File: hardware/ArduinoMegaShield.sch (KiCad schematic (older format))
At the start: 23 parts, among them P1 CONN_01X02, P10 CONN_01X02, P11 CONN_01X02, P12 CONN_01X02, P13 CONN_01X02, P14 CONN_01X02, P15 CONN_01X02, P16 CONN_01X02, P2 CONN_01X02, P3 CONN_01X02, P4 CONN_01X02, P5 CONN_01X02, P6 CONN_01X02, P7 CONN_01X02, P8 CONN_01X02, P9 CONN_01X02, U1 A4988, U2 A4988, U3 A4988

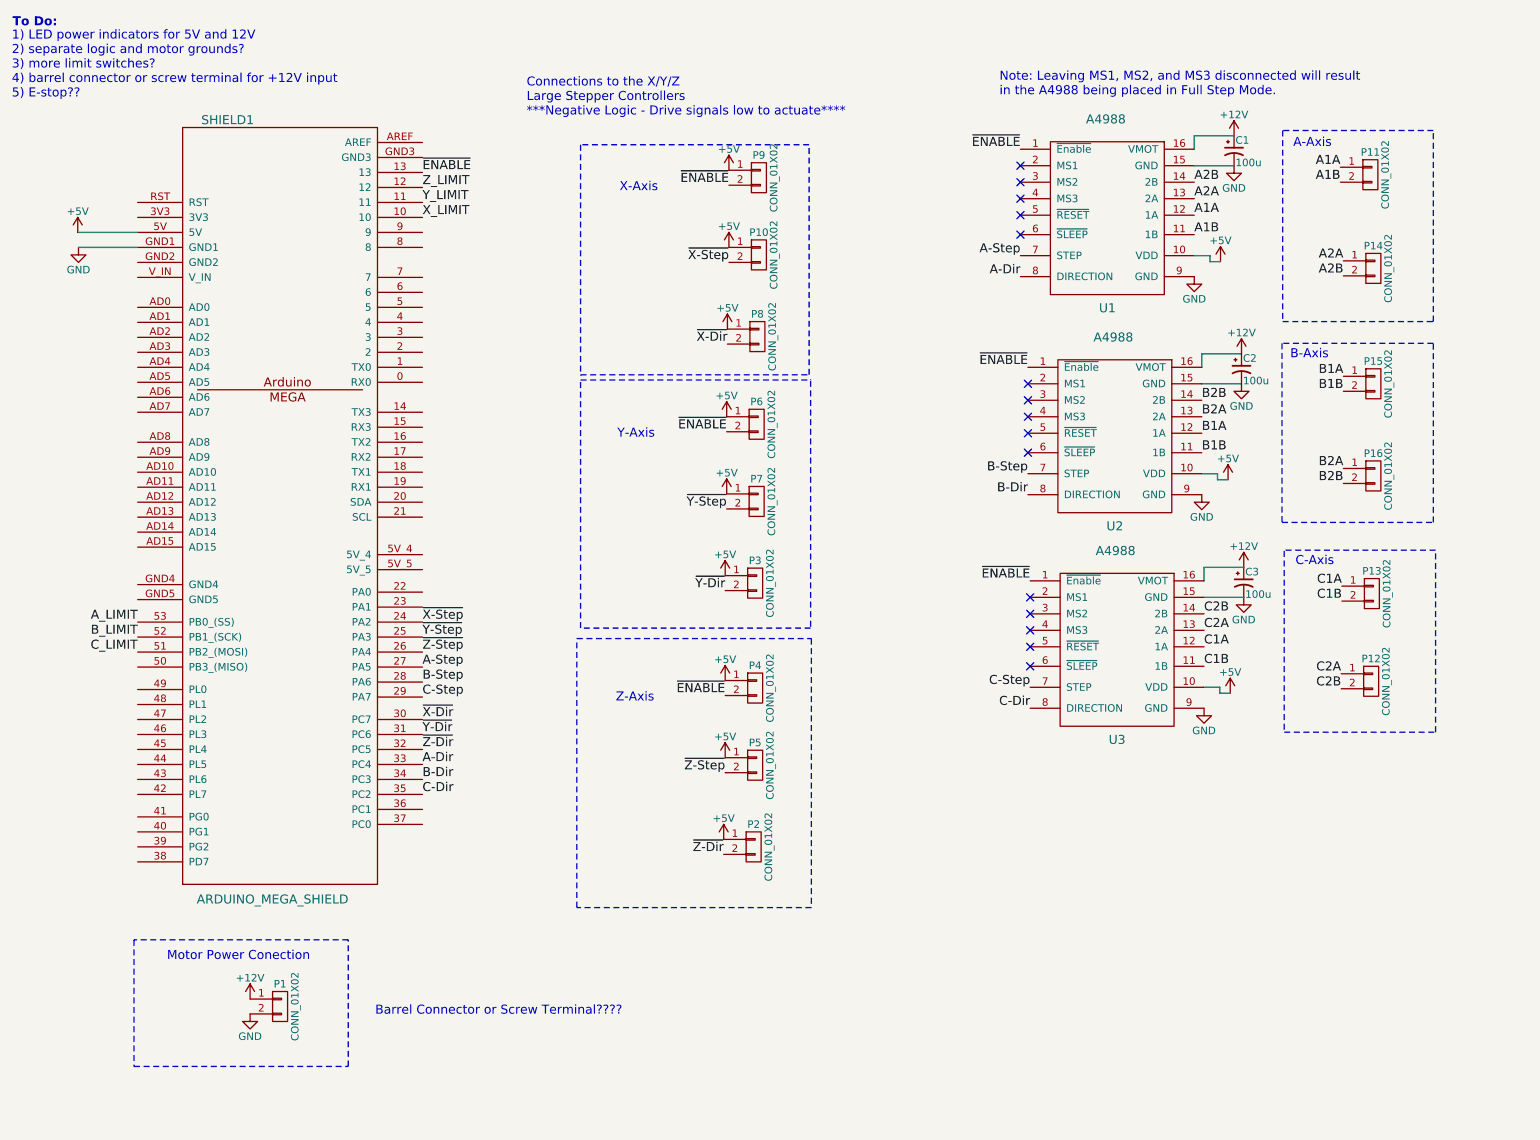
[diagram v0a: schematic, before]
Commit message: added microstepping NOPOP resistors and power indicator LEDs.  Assigned some footprints
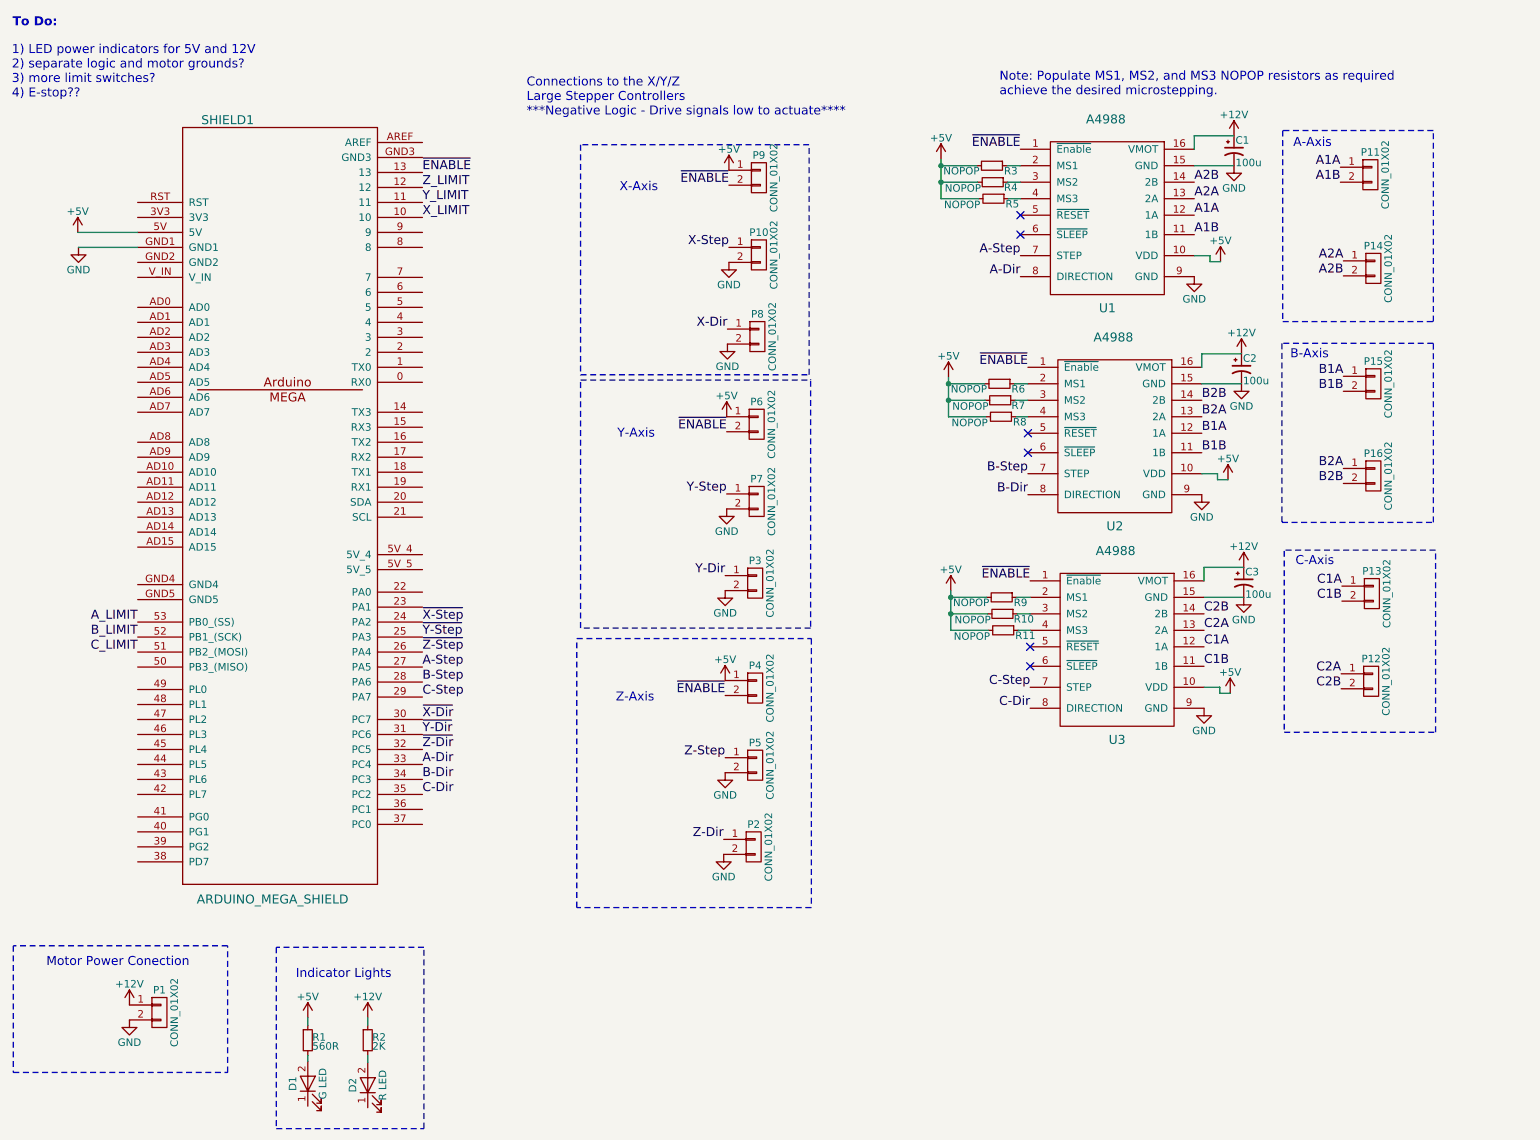
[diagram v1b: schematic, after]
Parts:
- added D1: G LED, LEDs:LED_0805, symbol LED
- added D2: R LED, LEDs:LED_0805, symbol LED
- added R1: 560R, Resistors_SMD:R_0805_HandSoldering, symbol R_Small
- added R10, R11, R3, R4, R5, R6, R7, R8, R9: NOPOP, Resistors_SMD:R_0805_HandSoldering, symbol R_Small
- added R2: 2K, Resistors_SMD:R_0805_HandSoldering, symbol R_Small
- P1, P10, P11, P12, P13, P14, P15, P16, P2, P3, P4, P5, P6, P7, P8, P9: footprint (none) -> Pin_Headers:Pin_Header_Straight_1x02
- SHIELD1: footprint (none) -> arduino-shields:ARDUINO_MEGA_SHIELD
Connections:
- net +12V: now also R2.1
- net +5V: now also R1.1, R10.2, R11.2, R3.2, R4.2, R5.2, R6.2, R7.2, R8.2, R9.2; no longer P10.1 (P1), P2.1 (P1), P3.1 (P1), P5.1 (P1), P7.1 (P1), P8.1 (P1)
- net GND: now also P10.2 (P2), P2.2 (P2), P3.2 (P2), P5.2 (P2), P7.2 (P2), P8.2 (P2)
- net ~X-Dir: no longer P8.2 (P2)
- net ~X-Step: no longer P10.2 (P2)
- net ~Y-Dir: no longer P3.2 (P2)
- net ~Y-Step: no longer P7.2 (P2)
- net ~Z-Dir: no longer P2.2 (P2)
- net ~Z-Step: no longer P5.2 (P2)
- net at U1.2 (MS1): now also R3.1
- net at U1.3 (MS2): now also R4.1
- net at U1.4 (MS3): now also R5.1
- net at U2.2 (MS1): now also R6.1
- net at U2.3 (MS2): now also R7.1
- net at U2.4 (MS3): now also R8.1
- net at U3.2 (MS1): now also R9.1
- net at U3.3 (MS2): now also R10.1
- net at U3.4 (MS3): now also R11.1
- new net: D1.2 (A), R1.2
- new net: D2.2 (A), R2.2
- new net X-Dir: P8.1 (P1)
- new net X-Step: P10.1 (P1)
- new net Y-Dir: P3.1 (P1)
- new net Y-Step: P7.1 (P1)
- new net Z-Dir: P2.1 (P1)
- new net Z-Step: P5.1 (P1)
- no-connect marks 15 -> 6
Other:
- note added: "1) LED power indicators for 5V and 12V\n2) separate logic and motor grounds?\n3) more limit switches?\n4) E-stop??"
- note added: "Indicator Lights"
- note added: "Note: Populate MS1, MS2, and MS3 NOPOP resistors as required\nachieve the desired microstepping."
- note removed: "1) LED power indicators for 5V and 12V\n2) separate logic and motor grounds?\n3) more limit switches?\n4) barrel connector or screw terminal for +12V input\n5) E-stop??"
- note removed: "Barrel Connector or Screw Terminal????"
- note removed: "Note: Leaving MS1, MS2, and MS3 disconnected will result\nin the A4988 being placed in Full Step Mode."
- moved on the sheet: P1

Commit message: correctly logic of steps/dir on shield output pins
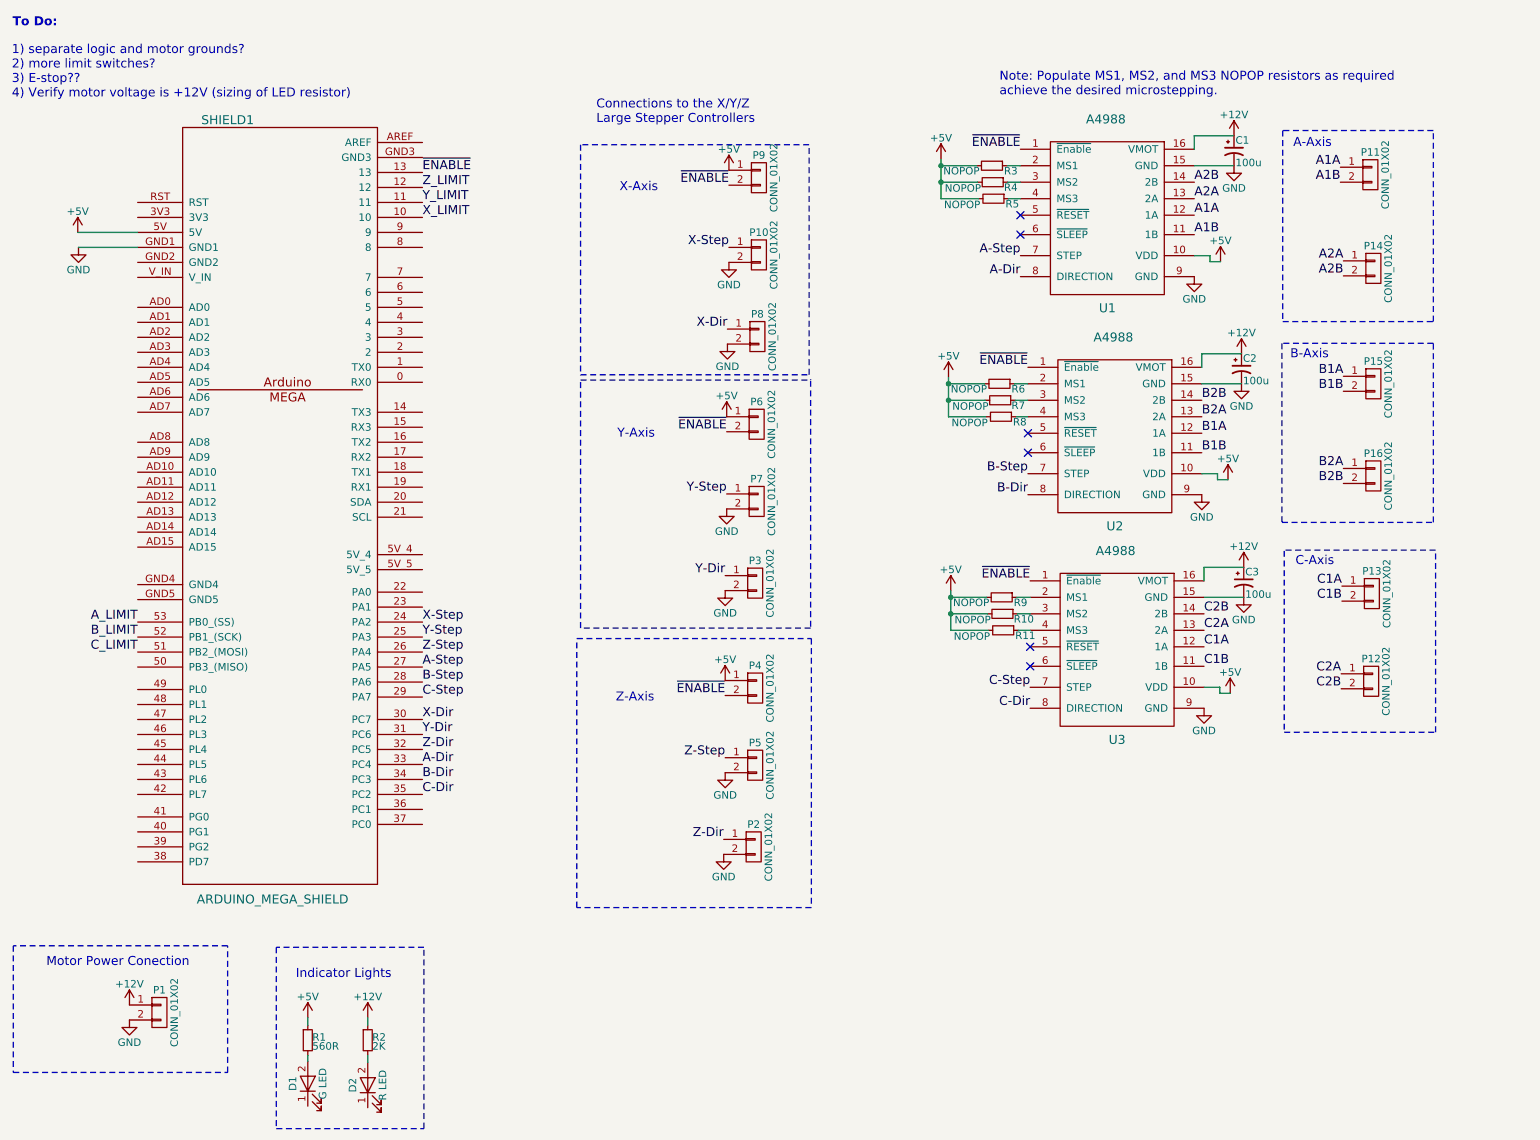
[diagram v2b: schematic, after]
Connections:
- net ~X-Dir is gone; now on net X-Dir: SHIELD1.30 (PC7)
- net ~X-Step is gone; now on net X-Step: SHIELD1.24 (PA2)
- net ~Y-Dir is gone; now on net Y-Dir: SHIELD1.31 (PC6)
- net ~Y-Step is gone; now on net Y-Step: SHIELD1.25 (PA3)
- net ~Z-Dir is gone; now on net Z-Dir: SHIELD1.32 (PC5)
- net ~Z-Step is gone; now on net Z-Step: SHIELD1.26 (PA4)
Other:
- note added: "1) separate logic and motor grounds?\n2) more limit switches?\n3) E-stop??\n4) Verify motor voltage is +12V (sizing of LED resistor)"
- note added: "Connections to the X/Y/Z\nLarge Stepper Controllers"
- note removed: "1) LED power indicators for 5V and 12V\n2) separate logic and motor grounds?\n3) more limit switches?\n4) E-stop??"
- note removed: "Connections to the X/Y/Z\nLarge Stepper Controllers\n***Negative Logic - Drive signals low to actuate****"
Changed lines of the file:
@@
 $EndComp
 Text Label 3450 4530 0    60   ~ 0
-~X-Step
+X-Step
 Text Label 3450 4630 0    60   ~ 0
-~Y-Step
+Y-Step
 Text Label 3450 4730 0    60   ~ 0
-~Z-Step
+Z-Step
 Text Label 3450 5180 0    60   ~ 0
-~X-Dir
+X-Dir
 Text Label 3450 5280 0    60   ~ 0
-~Y-Dir
+Y-Dir
 Text Label 3450 5380 0    60   ~ 0
-~Z-Dir
+Z-Dir
 Text Label 3450 1530 0    60   ~ 0
 ~ENABLE
-Text Notes 4145 1160 0    60   ~ 0
-Connections to the X/Y/Z\nLarge Stepper Controllers\n***Negative Logic - Drive signals low to actuate****
+Text Notes 4610 1210 0    60   ~ 0
+Connections to the X/Y/Z\nLarge Stepper Controllers
 $Comp
 L CONN_01X02 P9
@@
 To Do:
 Text Notes 710  1040 0    60   ~ 0
-1) LED power indicators for 5V and 12V\n2) separate logic and motor grounds?\n3) more limit switches?\n4) E-stop??
+1) separate logic and motor grounds?\n2) more limit switches?\n3) E-stop??\n4) Verify motor voltage is +12V (sizing of LED resistor)
 Text Notes 940  6835 0    60   ~ 0
 Motor Power Conection

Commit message: changed terminal connectors from dupont to 200 mil screw terminals
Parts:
- P1, P10, P11, P12, P13, P14, P15, P16, P2, P3, P4, P5, P6, P7, P8, P9: footprint Pin_Headers:Pin_Header_Straight_1x02 -> 6axis:Terminal_Block_200_mil
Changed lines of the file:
@@
 F 0 "P15" H 9795 3090 50  0000 C CNN
 F 1 "CONN_01X02" V 9895 2940 50  0000 C CNN
-F 2 "Pin_Headers:Pin_Header_Straight_1x02" H 9795 2940 50  0001 C CNN
+F 2 "6axis:Terminal_Block_200_mil" H 9795 2940 50  0001 C CNN
 F 3 "" H 9795 2940 50  0000 C CNN
 	1    9795 2940
@@
 F 0 "P16" H 9795 3705 50  0000 C CNN
 F 1 "CONN_01X02" V 9895 3555 50  0000 C CNN
-F 2 "Pin_Headers:Pin_Header_Straight_1x02" H 9795 3555 50  0001 C CNN
+F 2 "6axis:Terminal_Block_200_mil" H 9795 3555 50  0001 C CNN
 F 3 "" H 9795 3555 50  0000 C CNN
 	1    9795 3555
@@
 F 0 "P11" H 9775 1695 50  0000 C CNN
 F 1 "CONN_01X02" V 9875 1545 50  0000 C CNN
-F 2 "Pin_Headers:Pin_Header_Straight_1x02" H 9775 1545 50  0001 C CNN
+F 2 "6axis:Terminal_Block_200_mil" H 9775 1545 50  0001 C CNN
 F 3 "" H 9775 1545 50  0000 C CNN
 	1    9775 1545
@@
 F 0 "P14" H 9795 2320 50  0000 C CNN
 F 1 "CONN_01X02" V 9895 2170 50  0000 C CNN
-F 2 "Pin_Headers:Pin_Header_Straight_1x02" H 9795 2170 50  0001 C CNN
+F 2 "6axis:Terminal_Block_200_mil" H 9795 2170 50  0001 C CNN
 F 3 "" H 9795 2170 50  0000 C CNN
 	1    9795 2170
@@
 F 0 "P13" H 9785 4490 50  0000 C CNN
 F 1 "CONN_01X02" V 9885 4340 50  0000 C CNN
-F 2 "Pin_Headers:Pin_Header_Straight_1x02" H 9785 4340 50  0001 C CNN
+F 2 "6axis:Terminal_Block_200_mil" H 9785 4340 50  0001 C CNN
 F 3 "" H 9785 4340 50  0000 C CNN
 	1    9785 4340
@@
 F 0 "P12" H 9780 5075 50  0000 C CNN
 F 1 "CONN_01X02" V 9880 4925 50  0000 C CNN
-F 2 "Pin_Headers:Pin_Header_Straight_1x02" H 9780 4925 50  0001 C CNN
+F 2 "6axis:Terminal_Block_200_mil" H 9780 4925 50  0001 C CNN
 F 3 "" H 9780 4925 50  0000 C CNN
 	1    9780 4925
@@
 F 0 "P9" H 5695 1715 50  0000 C CNN
 F 1 "CONN_01X02" V 5795 1565 50  0000 C CNN
-F 2 "Pin_Headers:Pin_Header_Straight_1x02" H 5695 1565 50  0001 C CNN
+F 2 "6axis:Terminal_Block_200_mil" H 5695 1565 50  0001 C CNN
 F 3 "" H 5695 1565 50  0000 C CNN
 	1    5695 1565
@@
 F 0 "P10" H 5695 2230 50  0000 C CNN
 F 1 "CONN_01X02" V 5795 2080 50  0000 C CNN
-F 2 "Pin_Headers:Pin_Header_Straight_1x02" H 5695 2080 50  0001 C CNN
+F 2 "6axis:Terminal_Block_200_mil" H 5695 2080 50  0001 C CNN
 F 3 "" H 5695 2080 50  0000 C CNN
 	1    5695 2080
@@
 F 0 "P8" H 5685 2775 50  0000 C CNN
 F 1 "CONN_01X02" V 5785 2625 50  0000 C CNN
-F 2 "Pin_Headers:Pin_Header_Straight_1x02" H 5685 2625 50  0001 C CNN
+F 2 "6axis:Terminal_Block_200_mil" H 5685 2625 50  0001 C CNN
 F 3 "" H 5685 2625 50  0000 C CNN
 	1    5685 2625
@@
 F 0 "P6" H 5680 3360 50  0000 C CNN
 F 1 "CONN_01X02" V 5780 3210 50  0000 C CNN
-F 2 "Pin_Headers:Pin_Header_Straight_1x02" H 5680 3210 50  0001 C CNN
+F 2 "6axis:Terminal_Block_200_mil" H 5680 3210 50  0001 C CNN
 F 3 "" H 5680 3210 50  0000 C CNN
 	1    5680 3210
@@
 F 0 "P7" H 5680 3875 50  0000 C CNN
 F 1 "CONN_01X02" V 5780 3725 50  0000 C CNN
-F 2 "Pin_Headers:Pin_Header_Straight_1x02" H 5680 3725 50  0001 C CNN
+F 2 "6axis:Terminal_Block_200_mil" H 5680 3725 50  0001 C CNN
 F 3 "" H 5680 3725 50  0000 C CNN
 	1    5680 3725
@@
 F 0 "P3" H 5670 4420 50  0000 C CNN
 F 1 "CONN_01X02" V 5770 4270 50  0000 C CNN
-F 2 "Pin_Headers:Pin_Header_Straight_1x02" H 5670 4270 50  0001 C CNN
+F 2 "6axis:Terminal_Block_200_mil" H 5670 4270 50  0001 C CNN
 F 3 "" H 5670 4270 50  0000 C CNN
 	1    5670 4270
@@
 F 0 "P4" H 5670 5120 50  0000 C CNN
 F 1 "CONN_01X02" V 5770 4970 50  0000 C CNN
-F 2 "Pin_Headers:Pin_Header_Straight_1x02" H 5670 4970 50  0001 C CNN
+F 2 "6axis:Terminal_Block_200_mil" H 5670 4970 50  0001 C CNN
 F 3 "" H 5670 4970 50  0000 C CNN
 	1    5670 4970
@@
 F 0 "P5" H 5670 5635 50  0000 C CNN
 F 1 "CONN_01X02" V 5770 5485 50  0000 C CNN
-F 2 "Pin_Headers:Pin_Header_Straight_1x02" H 5670 5485 50  0001 C CNN
+F 2 "6axis:Terminal_Block_200_mil" H 5670 5485 50  0001 C CNN
 F 3 "" H 5670 5485 50  0000 C CNN
 	1    5670 5485
@@
 F 0 "P2" H 5660 6180 50  0000 C CNN
 F 1 "CONN_01X02" V 5760 6030 50  0000 C CNN
-F 2 "Pin_Headers:Pin_Header_Straight_1x02" H 5660 6030 50  0001 C CNN
+F 2 "6axis:Terminal_Block_200_mil" H 5660 6030 50  0001 C CNN
 F 3 "" H 5660 6030 50  0000 C CNN
 	1    5660 6030
@@
 F 0 "P1" H 1695 7285 50  0000 C CNN
 F 1 "CONN_01X02" V 1795 7135 50  0000 C CNN
-F 2 "Pin_Headers:Pin_Header_Straight_1x02" H 1695 7135 50  0001 C CNN
+F 2 "6axis:Terminal_Block_200_mil" H 1695 7135 50  0001 C CNN
 F 3 "" H 1695 7135 50  0000 C CNN
 	1    1695 7135

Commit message: added footprints for caps and motor drivers
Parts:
- C1, C2, C3: footprint (none) -> Capacitors_THT:C_Radial_D6.3_L11.2_P2.5; MPN (none) -> EEU-FM1E101
- U1, U2, U3: footprint (none) -> 6axis:A4988
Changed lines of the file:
@@
 F 0 "U1" H 8020 1175 60  0000 C CNN
 F 1 "A4988" H 8010 2435 60  0000 C CNN
-F 2 "" H 8020 1735 60  0001 C CNN
+F 2 "6axis:A4988" H 8020 1735 60  0001 C CNN
 F 3 "" H 8020 1735 60  0001 C CNN
 	1    8030 1805
@@
 F 0 "U2" H 8070 2630 60  0000 C CNN
 F 1 "A4988" H 8060 3890 60  0000 C CNN
-F 2 "" H 8070 3190 60  0001 C CNN
+F 2 "6axis:A4988" H 8070 3190 60  0001 C CNN
 F 3 "" H 8070 3190 60  0001 C CNN
 	1    8080 3260
@@
 F 0 "U3" H 8085 4055 60  0000 C CNN
 F 1 "A4988" H 8075 5315 60  0000 C CNN
-F 2 "" H 8085 4615 60  0001 C CNN
+F 2 "6axis:A4988" H 8085 4615 60  0001 C CNN
 F 3 "" H 8085 4615 60  0001 C CNN
 	1    8095 4685
@@
 F 0 "C1" H 8875 1455 50  0000 L CNN
 F 1 "100u" H 8875 1305 50  0000 L CNN
-F 2 "" H 8865 1385 50  0001 C CNN
-F 3 "" H 8865 1385 50  0000 C CNN
+F 2 "Capacitors_THT:C_Radial_D6.3_L11.2_P2.5" H 8865 1385 50  0001 C CNN
+F 3 "https://industrial.panasonic.com/cdbs/www-data/pdf/RDF0000/ABA0000C1018.pdf" H 8865 1385 50  0001 C CNN
 F 4 "Value" H 8865 1385 60  0001 C CNN "Fieldname"
+F 5 "EEU-FM1E101" H 8865 1385 60  0001 C CNN "MPN"
 	1    8865 1385
 	1    0    0    -1
@@
 F 0 "C2" H 8925 2910 50  0000 L CNN
 F 1 "100u" H 8925 2760 50  0000 L CNN
-F 2 "" H 8915 2840 50  0001 C CNN
-F 3 "" H 8915 2840 50  0000 C CNN
+F 2 "Capacitors_THT:C_Radial_D6.3_L11.2_P2.5" H 8915 2840 50  0001 C CNN
+F 3 "https://industrial.panasonic.com/cdbs/www-data/pdf/RDF0000/ABA0000C1018.pdf" H 8915 2840 50  0001 C CNN
 F 4 "Value" H 8915 2840 60  0001 C CNN "Fieldname"
+F 5 "EEU-FM1E101" H 8915 2840 60  0001 C CNN "MPN"
 	1    8915 2840
 	1    0    0    -1
@@
 F 0 "C3" H 8940 4335 50  0000 L CNN
 F 1 "100u" H 8940 4185 50  0000 L CNN
-F 2 "" H 8930 4265 50  0001 C CNN
-F 3 "" H 8930 4265 50  0000 C CNN
+F 2 "Capacitors_THT:C_Radial_D6.3_L11.2_P2.5" H 8930 4265 50  0001 C CNN
+F 3 "https://industrial.panasonic.com/cdbs/www-data/pdf/RDF0000/ABA0000C1018.pdf" H 8930 4265 50  0001 C CNN
 F 4 "Value" H 8930 4265 60  0001 C CNN "Fieldname"
+F 5 "EEU-FM1E101" H 8930 4265 60  0001 C CNN "MPN"
 	1    8930 4265
 	1    0    0    -1
